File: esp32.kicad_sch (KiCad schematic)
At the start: 13 parts, among them IC3 ESP32-C3-WROOM-02-N4, J5 UART, J6 ToSSR, Q1 BSS138, SW1 SW_MEC_5G

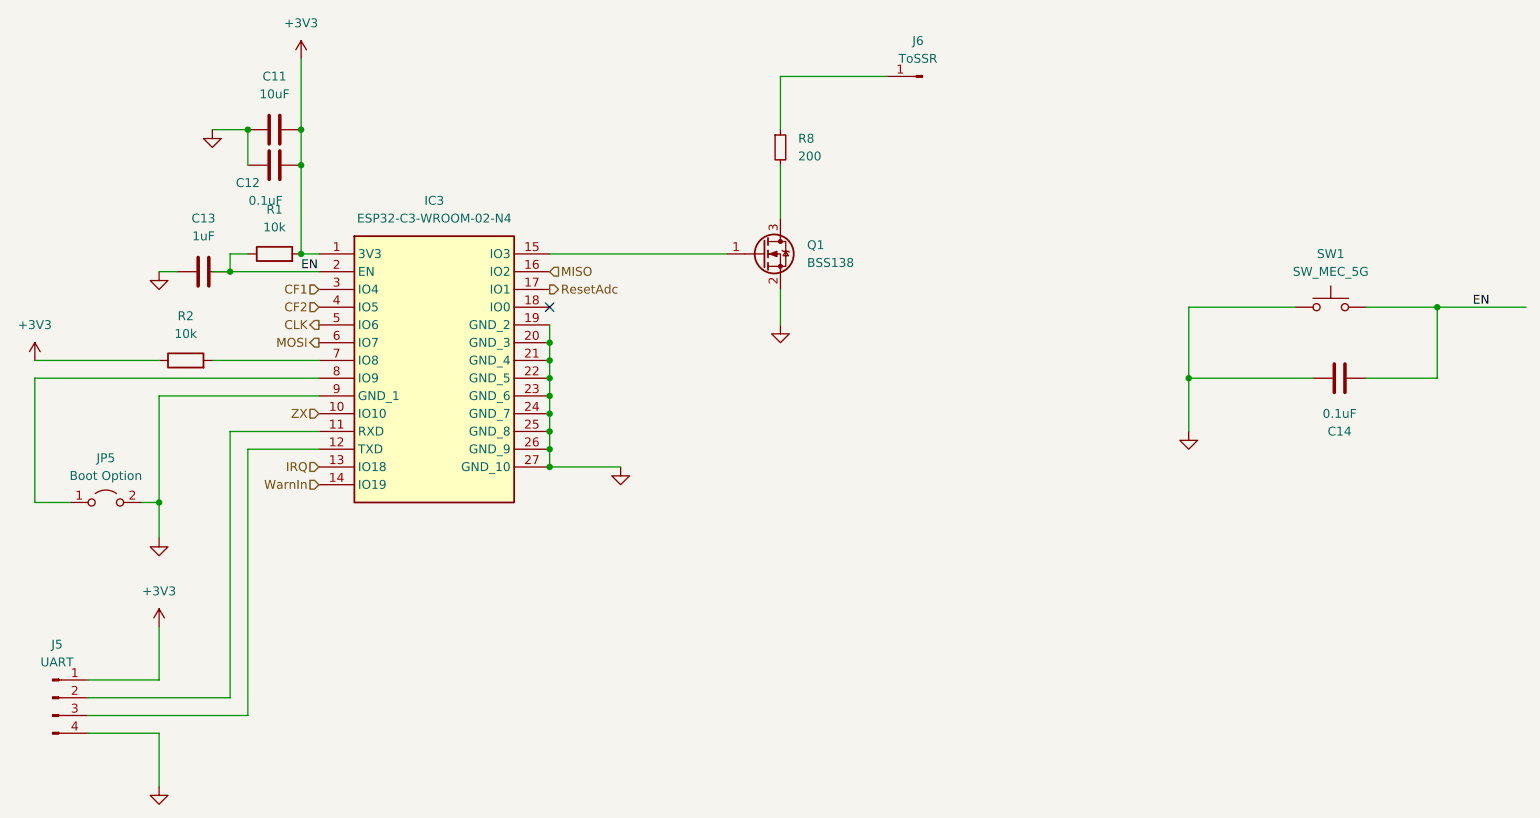
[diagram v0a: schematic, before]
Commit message: fix: init symbols references
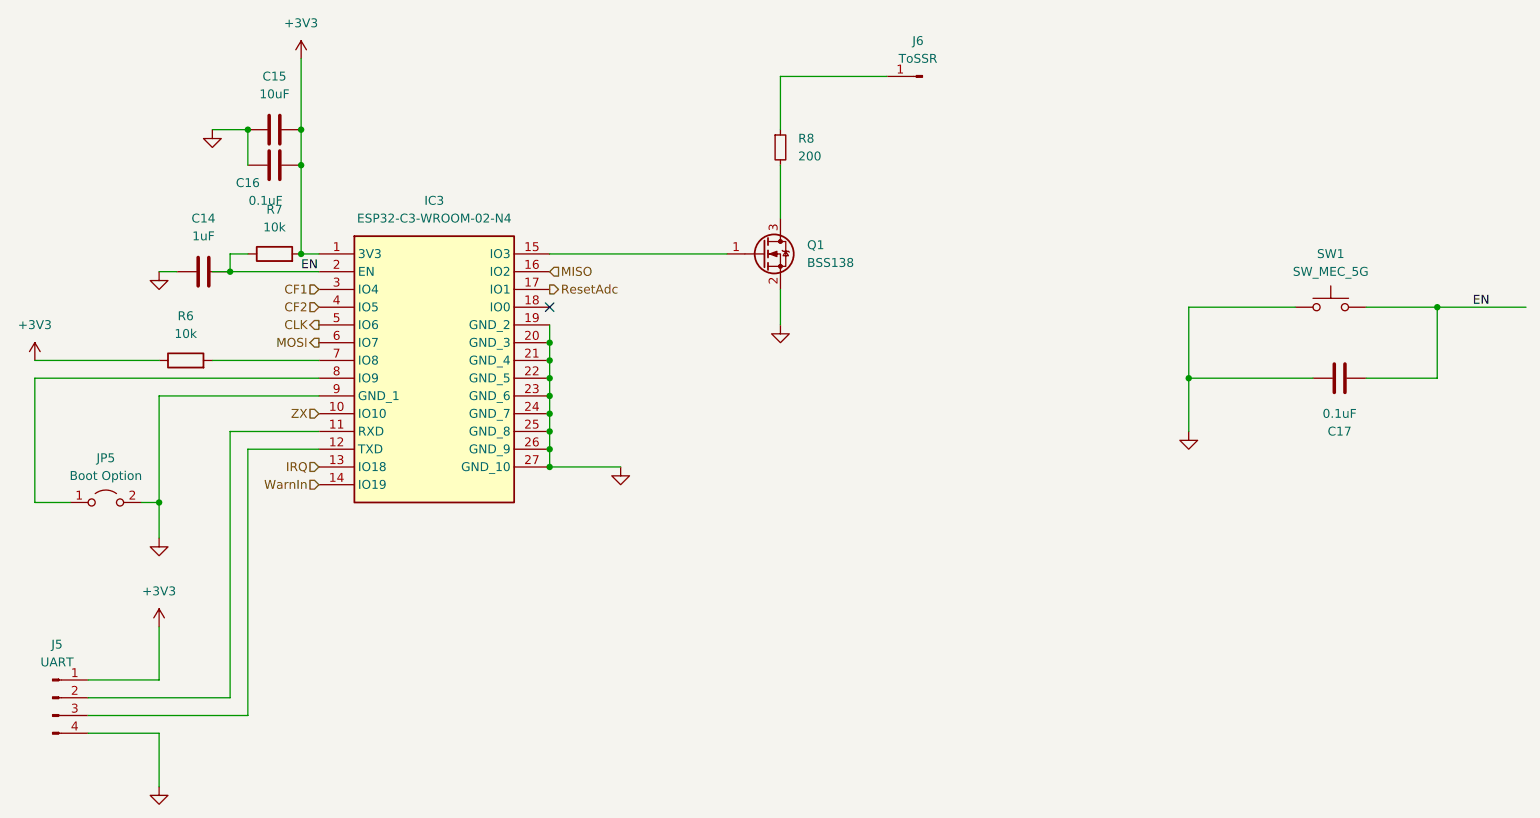
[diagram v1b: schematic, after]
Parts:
- renumbered C13 to C14, C11 to C15, C12 to C16, C14 to C17, R2 to R6, R1 to R7
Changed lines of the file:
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@@
   (symbol (lib_id "Device:R") (at 59.69 81.28 90) (unit 1)
     (in_bom yes) (on_board yes) (dnp no) (fields_autoplaced)
-    (property "Reference" "R1" (at 59.69 74.93 90)
+    (property "Reference" "R7" (at 59.69 74.93 90)
       (effects (font (size 1.27 1.27)))
     )
@@
       (project "pv_router"
         (path "/08ef31dc-81c2-4bcd-8336-e62c344e451e/5b2a06a5-fb5f-4aba-bfde-32c85173e89f"
-          (reference "R1") (unit 1)
+          (reference "R7") (unit 1)
         )
       )
@@
   (symbol (lib_id "power:+3V3") (at 43.18 134.62 0) (unit 1)
     (in_bom yes) (on_board yes) (dnp no) (fields_autoplaced)
-    (property "Reference" "#PWR025" (at 43.18 138.43 0)
+    (property "Reference" "#PWR026" (at 43.18 138.43 0)
       (effects (font (size 1.27 1.27)) hide)
     )
@@
       (project "pv_router"
         (path "/08ef31dc-81c2-4bcd-8336-e62c344e451e/5b2a06a5-fb5f-4aba-bfde-32c85173e89f"
-          (reference "#PWR025") (unit 1)
+          (reference "#PWR026") (unit 1)
         )
       )
@@
   (symbol (lib_id "Device:R") (at 46.99 96.52 90) (unit 1)
     (in_bom yes) (on_board yes) (dnp no) (fields_autoplaced)
-    (property "Reference" "R2" (at 46.99 90.17 90)
+    (property "Reference" "R6" (at 46.99 90.17 90)
       (effects (font (size 1.27 1.27)))
     )
@@
       (project "pv_router"
         (path "/08ef31dc-81c2-4bcd-8336-e62c344e451e/5b2a06a5-fb5f-4aba-bfde-32c85173e89f"
-          (reference "R2") (unit 1)
+          (reference "R6") (unit 1)
         )
       )
@@
   (symbol (lib_id "power:+3V3") (at 63.5 53.34 0) (unit 1)
     (in_bom yes) (on_board yes) (dnp no) (fields_autoplaced)
-    (property "Reference" "#PWR018" (at 63.5 57.15 0)
+    (property "Reference" "#PWR029" (at 63.5 57.15 0)
       (effects (font (size 1.27 1.27)) hide)
     )
@@
       (project "pv_router"
         (path "/08ef31dc-81c2-4bcd-8336-e62c344e451e/5b2a06a5-fb5f-4aba-bfde-32c85173e89f"
-          (reference "#PWR018") (unit 1)
+          (reference "#PWR029") (unit 1)
         )
       )
@@
   (symbol (lib_id "power:GND") (at 43.18 157.48 0) (unit 1)
     (in_bom yes) (on_board yes) (dnp no) (fields_autoplaced)
-    (property "Reference" "#PWR023" (at 43.18 163.83 0)
+    (property "Reference" "#PWR027" (at 43.18 163.83 0)
       (effects (font (size 1.27 1.27)) hide)
     )
@@
       (project "pv_router"
         (path "/08ef31dc-81c2-4bcd-8336-e62c344e451e/5b2a06a5-fb5f-4aba-bfde-32c85173e89f"
-          (reference "#PWR023") (unit 1)
+          (reference "#PWR027") (unit 1)
         )
       )
@@
   (symbol (lib_id "Device:C") (at 49.53 83.82 90) (unit 1)
     (in_bom yes) (on_board yes) (dnp no) (fields_autoplaced)
-    (property "Reference" "C13" (at 49.53 76.2 90)
+    (property "Reference" "C14" (at 49.53 76.2 90)
       (effects (font (size 1.27 1.27)))
     )
@@
       (project "pv_router"
         (path "/08ef31dc-81c2-4bcd-8336-e62c344e451e/5b2a06a5-fb5f-4aba-bfde-32c85173e89f"
-          (reference "C13") (unit 1)
+          (reference "C14") (unit 1)
         )
       )
@@
   (symbol (lib_id "power:GND") (at 43.18 83.82 0) (unit 1)
     (in_bom yes) (on_board yes) (dnp no) (fields_autoplaced)
-    (property "Reference" "#PWR021" (at 43.18 90.17 0)
+    (property "Reference" "#PWR024" (at 43.18 90.17 0)
       (effects (font (size 1.27 1.27)) hide)
     )
@@
       (project "pv_router"
         (path "/08ef31dc-81c2-4bcd-8336-e62c344e451e/5b2a06a5-fb5f-4aba-bfde-32c85173e89f"
-          (reference "#PWR021") (unit 1)
+          (reference "#PWR024") (unit 1)
         )
       )
@@
   (symbol (lib_id "power:GND") (at 190.5 106.68 0) (unit 1)
     (in_bom yes) (on_board yes) (dnp no) (fields_autoplaced)
-    (property "Reference" "#PWR022" (at 190.5 113.03 0)
+    (property "Reference" "#PWR032" (at 190.5 113.03 0)
       (effects (font (size 1.27 1.27)) hide)
     )
@@
       (project "pv_router"
         (path "/08ef31dc-81c2-4bcd-8336-e62c344e451e/5b2a06a5-fb5f-4aba-bfde-32c85173e89f"
-          (reference "#PWR022") (unit 1)
+          (reference "#PWR032") (unit 1)
         )
       )
@@
   (symbol (lib_id "power:GND") (at 43.18 121.92 0) (unit 1)
     (in_bom yes) (on_board yes) (dnp no) (fields_autoplaced)
-    (property "Reference" "#PWR019" (at 43.18 128.27 0)
+    (property "Reference" "#PWR025" (at 43.18 128.27 0)
       (effects (font (size 1.27 1.27)) hide)
     )
@@
       (project "pv_router"
         (path "/08ef31dc-81c2-4bcd-8336-e62c344e451e/5b2a06a5-fb5f-4aba-bfde-32c85173e89f"
-          (reference "#PWR019") (unit 1)
+          (reference "#PWR025") (unit 1)
         )
       )
@@
   (symbol (lib_id "Device:C") (at 59.69 63.5 90) (unit 1)
     (in_bom yes) (on_board yes) (dnp no) (fields_autoplaced)
-    (property "Reference" "C11" (at 59.69 55.88 90)
+    (property "Reference" "C15" (at 59.69 55.88 90)
       (effects (font (size 1.27 1.27)))
     )
@@
       (project "pv_router"
         (path "/08ef31dc-81c2-4bcd-8336-e62c344e451e/5b2a06a5-fb5f-4aba-bfde-32c85173e89f"
-          (reference "C11") (unit 1)
+          (reference "C15") (unit 1)
         )
       )
@@
   (symbol (lib_id "power:GND") (at 109.22 111.76 0) (unit 1)
     (in_bom yes) (on_board yes) (dnp no) (fields_autoplaced)
-    (property "Reference" "#PWR017" (at 109.22 118.11 0)
+    (property "Reference" "#PWR030" (at 109.22 118.11 0)
       (effects (font (size 1.27 1.27)) hide)
     )
@@
       (project "pv_router"
         (path "/08ef31dc-81c2-4bcd-8336-e62c344e451e/5b2a06a5-fb5f-4aba-bfde-32c85173e89f"
-          (reference "#PWR017") (unit 1)
+          (reference "#PWR030") (unit 1)
         )
       )
@@
   (symbol (lib_id "power:GND") (at 50.8 63.5 0) (unit 1)
     (in_bom yes) (on_board yes) (dnp no) (fields_autoplaced)
-    (property "Reference" "#PWR020" (at 50.8 69.85 0)
+    (property "Reference" "#PWR028" (at 50.8 69.85 0)
       (effects (font (size 1.27 1.27)) hide)
     )
@@
       (project "pv_router"
         (path "/08ef31dc-81c2-4bcd-8336-e62c344e451e/5b2a06a5-fb5f-4aba-bfde-32c85173e89f"
-          (reference "#PWR020") (unit 1)
+          (reference "#PWR028") (unit 1)
         )
       )
@@
   (symbol (lib_id "Device:C") (at 212.09 99.06 90) (unit 1)
     (in_bom yes) (on_board yes) (dnp no)
-    (property "Reference" "C14" (at 212.09 106.68 90)
+    (property "Reference" "C17" (at 212.09 106.68 90)
       (effects (font (size 1.27 1.27)))
     )
@@
       (project "pv_router"
         (path "/08ef31dc-81c2-4bcd-8336-e62c344e451e/5b2a06a5-fb5f-4aba-bfde-32c85173e89f"
-          (reference "C14") (unit 1)
+          (reference "C17") (unit 1)
         )
       )
@@
   (symbol (lib_id "power:+3V3") (at 25.4 96.52 0) (unit 1)
     (in_bom yes) (on_board yes) (dnp no) (fields_autoplaced)
-    (property "Reference" "#PWR024" (at 25.4 100.33 0)
+    (property "Reference" "#PWR023" (at 25.4 100.33 0)
       (effects (font (size 1.27 1.27)) hide)
     )
@@
       (project "pv_router"
         (path "/08ef31dc-81c2-4bcd-8336-e62c344e451e/5b2a06a5-fb5f-4aba-bfde-32c85173e89f"
-          (reference "#PWR024") (unit 1)
+          (reference "#PWR023") (unit 1)
         )
       )
@@
   (symbol (lib_id "Device:C") (at 59.69 68.58 90) (unit 1)
     (in_bom yes) (on_board yes) (dnp no)
-    (property "Reference" "C12" (at 55.88 71.12 90)
+    (property "Reference" "C16" (at 55.88 71.12 90)
       (effects (font (size 1.27 1.27)))
     )
@@
       (project "pv_router"
         (path "/08ef31dc-81c2-4bcd-8336-e62c344e451e/5b2a06a5-fb5f-4aba-bfde-32c85173e89f"
-          (reference "C12") (unit 1)
+          (reference "C16") (unit 1)
         )
       )
@@
   (symbol (lib_id "power:GND") (at 132.08 91.44 0) (unit 1)
     (in_bom yes) (on_board yes) (dnp no) (fields_autoplaced)
-    (property "Reference" "#PWR032" (at 132.08 97.79 0)
+    (property "Reference" "#PWR031" (at 132.08 97.79 0)
       (effects (font (size 1.27 1.27)) hide)
     )
@@
       (project "pv_router"
         (path "/08ef31dc-81c2-4bcd-8336-e62c344e451e/5b2a06a5-fb5f-4aba-bfde-32c85173e89f"
-          (reference "#PWR032") (unit 1)
-        )
-      )
+          (reference "#PWR031") (unit 1)
+        )
+      )

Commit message: fix: assigned FP for ICs
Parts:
- IC3: footprint ESP32C3WROOM02N4 -> ESP32-C3-WROOM-02-N4:ESP32C3WROOM02N4
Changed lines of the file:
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@@
       (effects (font (size 1.27 1.27)))
     )
-    (property "Footprint" "ESP32C3WROOM02N4" (at 95.25 176.2 0)
+    (property "Footprint" "ESP32-C3-WROOM-02-N4:ESP32C3WROOM02N4" (at 95.25 176.2 0)
       (effects (font (size 1.27 1.27)) (justify left top) hide)
     )

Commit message: stagged
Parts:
- R6, R7, R8: footprint Resistor_THT:R_Array_SIP4 -> Resistor_THT:R_Axial_DIN0207_L6.3mm_D2.5mm_P7.62mm_Horizontal
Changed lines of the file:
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@@
       (effects (font (size 1.27 1.27)))
     )
-    (property "Footprint" "Resistor_THT:R_Array_SIP4" (at 59.69 83.058 90)
+    (property "Footprint" "Resistor_THT:R_Axial_DIN0207_L6.3mm_D2.5mm_P7.62mm_Horizontal" (at 59.69 83.058 90)
       (effects (font (size 1.27 1.27)) hide)
     )
@@
       (effects (font (size 1.27 1.27)))
     )
-    (property "Footprint" "Resistor_THT:R_Array_SIP4" (at 46.99 98.298 90)
+    (property "Footprint" "Resistor_THT:R_Axial_DIN0207_L6.3mm_D2.5mm_P7.62mm_Horizontal" (at 46.99 98.298 90)
       (effects (font (size 1.27 1.27)) hide)
     )
@@
       (effects (font (size 1.27 1.27)) (justify left))
     )
-    (property "Footprint" "Resistor_THT:R_Array_SIP4" (at 132.08 66.04 0)
+    (property "Footprint" "Resistor_THT:R_Axial_DIN0207_L6.3mm_D2.5mm_P7.62mm_Horizontal" (at 132.08 66.04 0)
       (effects (font (size 1.27 1.27)) hide)
     )

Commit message: FP: first FP update
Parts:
- C14: footprint Capacitor_SMD:C_0805_2012Metric_Pad1.18x1.45mm_HandSolder -> Capacitor_SMD:C_0603_1608Metric
- Q1: Manufacturer_Name (none) -> 1 dispo
- SW1: footprint Button_Switch_SMD:SW_MEC_5GSH9 -> Button_Switch_SMD:SW_SPST_EVQQ2; Manufacturer_Name (none) -> 4 dispo
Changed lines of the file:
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@@
       (effects (font (size 1.27 1.27)))
     )
-    (property "Footprint" "Button_Switch_SMD:SW_MEC_5GSH9" (at 210.82 83.82 0)
+    (property "Footprint" "Button_Switch_SMD:SW_SPST_EVQQ2" (at 210.82 83.82 0)
       (effects (font (size 1.27 1.27)) hide)
     )
     (property "Datasheet" "http://www.apem.com/int/index.php?controller=attachment&id_attachment=488" (at 210.82 83.82 0)
+      (effects (font (size 1.27 1.27)) hide)
+    )
+    (property "Manufacturer_Name" "4 dispo" (at 210.82 88.9 0)
       (effects (font (size 1.27 1.27)) hide)
     )
@@
       (effects (font (size 1.27 1.27)))
     )
-    (property "Footprint" "Capacitor_SMD:C_0805_2012Metric_Pad1.18x1.45mm_HandSolder" (at 53.34 82.8548 0)
-      (effects (font (size 1.27 1.27)) hide)
-    )
-    (property "Datasheet" "~" (at 49.53 83.82 0)
+    (property "Footprint" "Capacitor_SMD:C_0603_1608Metric" (at 53.34 82.8548 0)
+      (effects (font (size 1.27 1.27)) hide)
+    )
+    (property "Datasheet" "2 dispo en x7r 547-113-17" (at 49.53 83.82 0)
       (effects (font (size 1.27 1.27)) hide)
     )
@@
       (effects (font (size 1.27 1.27)) (justify left) hide)
     )
-    (pin "1")
+    (property "Manufacturer_Name" "1 dispo" (at 129.54 81.28 0)
+      (effects (font (size 1.27 1.27)) hide)
+    )
+    (pin "1")

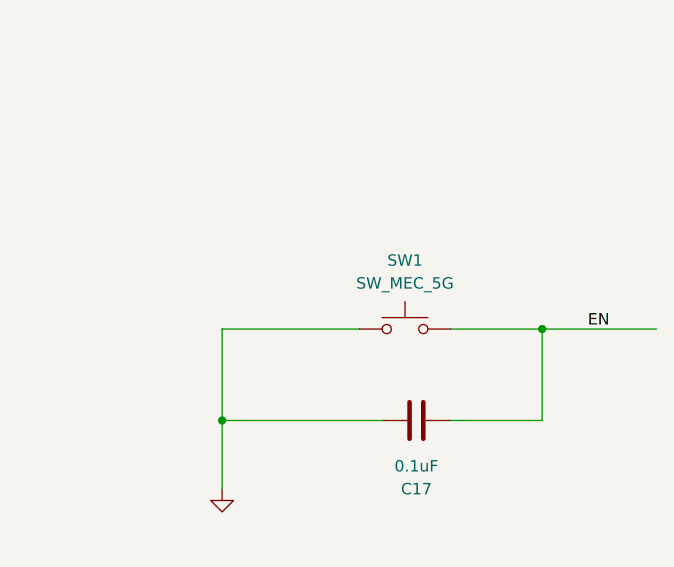
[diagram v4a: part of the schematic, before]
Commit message: FP: update SW1 FP
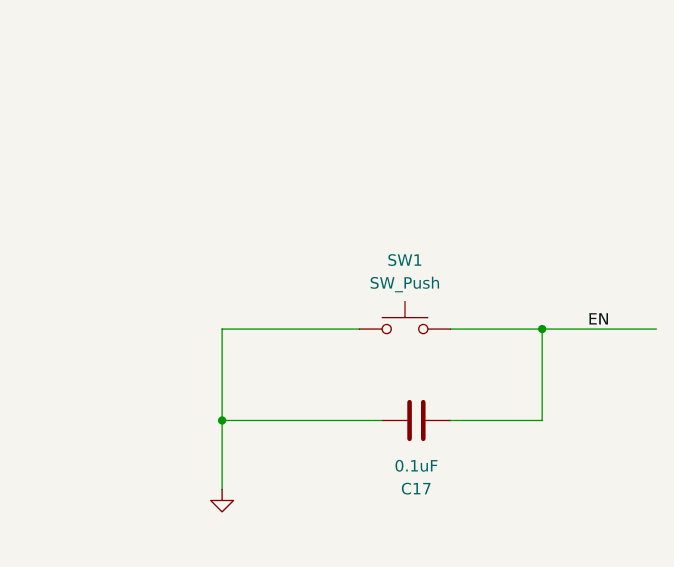
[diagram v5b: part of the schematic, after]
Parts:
- removed SW1: SW_MEC_5G, Button_Switch_SMD:SW_SPST_EVQQ2, symbol Switch:SW_MEC_5G
- added SW1: SW_Push, Button_Switch_SMD:SW_SPST_EVQQ2, symbol Switch:SW_Push
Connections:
- net EN: now also SW1.2
- net GND: now also SW1.1
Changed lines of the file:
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@@
-    )
-  )
-  (symbol (lib_id "Switch:SW_MEC_5G") (at 210.82 88.9 0) (unit 1)
-    (in_bom yes) (on_board yes) (dnp no) (fields_autoplaced)
-    (property "Reference" "SW1" (at 210.82 81.28 0)
-      (effects (font (size 1.27 1.27)))
-    )
-    (property "Value" "SW_MEC_5G" (at 210.82 83.82 0)
-      (effects (font (size 1.27 1.27)))
-    )
-    (property "Footprint" "Button_Switch_SMD:SW_SPST_EVQQ2" (at 210.82 83.82 0)
-      (effects (font (size 1.27 1.27)) hide)
-    )
-    (property "Datasheet" "http://www.apem.com/int/index.php?controller=attachment&id_attachment=488" (at 210.82 83.82 0)
-      (effects (font (size 1.27 1.27)) hide)
-    )
-    (property "Manufacturer_Name" "4 dispo" (at 210.82 88.9 0)
-      (effects (font (size 1.27 1.27)) hide)
-    )
-    (pin "3")
-    (pin "2")
-    (pin "1")
-    (pin "4")
-    (instances
-      (project "pv_router"
-        (path "/08ef31dc-81c2-4bcd-8336-e62c344e451e/5b2a06a5-fb5f-4aba-bfde-32c85173e89f"
-          (reference "SW1") (unit 1)
-        )
-      )
     )
   )
@@
         )
       )
+    )
+  )
+  (symbol (lib_id "Switch:SW_Push") (at 210.82 88.9 0) (unit 1)
+    (in_bom yes) (on_board yes) (dnp no) (fields_autoplaced)
+    (property "Reference" "SW1" (at 210.82 81.28 0)
+      (effects (font (size 1.27 1.27)))
+    )
+    (property "Value" "SW_Push" (at 210.82 83.82 0)
+      (effects (font (size 1.27 1.27)))
+    )
+    (property "Footprint" "Button_Switch_SMD:SW_SPST_EVQQ2" (at 210.82 83.82 0)
+      (effects (font (size 1.27 1.27)) hide)
+    )
+    (property "Datasheet" "~" (at 210.82 83.82 0)
+      (effects (font (size 1.27 1.27)) hide)
+    )
+    (pin "2")
+    (pin "1")
+    (instances
+      (project "pv_router"
+        (path "/08ef31dc-81c2-4bcd-8336-e62c344e451e/5b2a06a5-fb5f-4aba-bfde-32c85173e89f"
+          (reference "SW1") (unit 1)
+        )
+      )

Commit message: FP: associate FP except jumpers
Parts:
- C15, C16, C17: footprint Capacitor_SMD:C_0805_2012Metric_Pad1.18x1.45mm_HandSolder -> Capacitor_SMD:C_0805_2012Metric
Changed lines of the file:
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@@
       (effects (font (size 1.27 1.27)) (justify left top) hide)
     )
-    (property "Datasheet" "https://www.mouser.ch/datasheet/2/891/Espressif_ESP32_C3_WROOM_02-2006871.pdf" (at 95.25 276.2 0)
+    (property "Datasheet" "ok :1" (at 95.25 276.2 0)
       (effects (font (size 1.27 1.27)) (justify left top) hide)
     )
@@
       (effects (font (size 1.27 1.27)) hide)
     )
-    (property "Datasheet" "ok" (at 132.08 66.04 0)
+    (property "Datasheet" "dispo 180 ou 220" (at 132.08 66.04 0)
       (effects (font (size 1.27 1.27)) hide)
     )
@@
       (effects (font (size 1.27 1.27)))
     )
-    (property "Footprint" "Capacitor_SMD:C_0805_2012Metric_Pad1.18x1.45mm_HandSolder" (at 63.5 62.5348 0)
-      (effects (font (size 1.27 1.27)) hide)
-    )
-    (property "Datasheet" "~" (at 59.69 63.5 0)
+    (property "Footprint" "Capacitor_SMD:C_0805_2012Metric" (at 63.5 62.5348 0)
+      (effects (font (size 1.27 1.27)) hide)
+    )
+    (property "Datasheet" "ok: 2" (at 59.69 63.5 0)
       (effects (font (size 1.27 1.27)) hide)
     )
@@
       (effects (font (size 1.27 1.27)))
     )
-    (property "Footprint" "Capacitor_SMD:C_0805_2012Metric_Pad1.18x1.45mm_HandSolder" (at 215.9 98.0948 0)
-      (effects (font (size 1.27 1.27)) hide)
-    )
-    (property "Datasheet" "~" (at 212.09 99.06 0)
+    (property "Footprint" "Capacitor_SMD:C_0805_2012Metric" (at 215.9 98.0948 0)
+      (effects (font (size 1.27 1.27)) hide)
+    )
+    (property "Datasheet" "ok : 4" (at 212.09 99.06 0)
       (effects (font (size 1.27 1.27)) hide)
     )
@@
       (effects (font (size 1.27 1.27)))
     )
-    (property "Footprint" "Capacitor_SMD:C_0805_2012Metric_Pad1.18x1.45mm_HandSolder" (at 63.5 67.6148 0)
-      (effects (font (size 1.27 1.27)) hide)
-    )
-    (property "Datasheet" "~" (at 59.69 68.58 0)
-      (effects (font (size 1.27 1.27)) hide)
-    )
+    (property "Footprint" "Capacitor_SMD:C_0805_2012Metric" (at 63.5 67.6148 0)
+      (effects (font (size 1.27 1.27)) hide)
+    )
+    (property "Datasheet" "ok : 4" (at 59.69 68.58 0)
+      (effects (font (size 1.27 1.27)) hide)
+    )
